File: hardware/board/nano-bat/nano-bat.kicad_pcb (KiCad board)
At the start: 2 copper layers, 160 x 106.7 mm, 97 parts, among them J101 Barrel_Jack_Switch, J102 USB_B_Mini, J103 Screw_Terminal_01x02, J104 Conn_01x02, J201 Conn_2Rows-45Pins, J301 Conn_ARM_JTAG_SWD_10, J302 Conn_01x10, J303 Conn_01x10, Q101 Q_PMOS_GSD, Q501 Q_PMOS_GSD, Q502 Q_NMOS_GSD, Q503 Q_NMOS_GSD, SW301 SW_Push, SW302 SW_Push, SW303 SW_Push, SW304 SW_Push, U201 AP3032, U301 M95256-WMN6P, U302 STM32L452CEUx, U401 LTC2942, U501 MIC2104YML-TR, U502 MCP1702

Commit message: Adding test points, initial board outline
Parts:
- added F401: Polyfuse, Fuse:Fuse_0603_1608Metric, F.Cu at (227.3, 78.2)
- added F501: Polyfuse, Fuse:Fuse_1812_4532Metric, F.Cu at (222.9, 120.7)
- added R315: 40.2k, Resistor_SMD:R_0603_1608Metric, F.Cu at (180.1, 23.0)
- added R316: 10k, Resistor_SMD:R_0603_1608Metric, F.Cu at (180.1, 25.5)
- added TP301: TestPoint, TestPoint:TestPoint_Plated_Hole_D2.0mm, F.Cu at (175.8, 24.1)
- J102: footprint footprints:USB-MICRO-B-HIROSE-UX60-MB-5S8 -> Connector_USB:USB_Mini-B_Lumberg_2486_01_Horizontal
- R406: footprint footprints:SM6227 -> Resistor_SMD:R_1206_3216Metric
- U201: moved to B.Cu
- moved C202 185.7 mm to (121.1, 134.0)
- moved D201 185.7 mm to (117.0, 131.7)
- moved L201 185.7 mm to (112.6, 131.7)
- moved R201 185.7 mm to (121.1, 131.4)
- moved C201 185.7 mm to (125.1, 131.4)
- moved U302 181.7 mm to (143.9, 33.7)
- moved U201 171.2 mm to (120.7, 123.8)
- moved J102 150.4 mm to (178.4, 58.4), turned to 180 degrees
- moved J104 140.0 mm to (196.2, 74.3), turned to 90 degrees
- moved J301 128.0 mm to (143.5, 22.9)
- moved J103 124.3 mm to (196.2, 86.4), turned to 90 degrees
- moved C302 117.9 mm to (155.4, 41.0)
- moved C305 117.9 mm to (155.4, 38.5)
- moved C311 117.9 mm to (164.0, 41.5)
- moved C301 117.9 mm to (164.6, 31.5)
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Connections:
- C201 pad 1: +2V8 -> GND
- C202 pad 2: +2V8 -> GND
- C301 pad 2: +2V8 -> GND
- C302 pad 2: +2V8 -> GND
- C303 pad 2: +2V8 -> GND
- C304 pad 2: +2V8 -> GND
- C305 pad 1: +2V8 -> GND
- C308 pad 2: +2V8 -> GND
- C309 pad 2: +2V8 -> GND
- C310 pad 2: +2V8 -> GND
- C311 pad 2: +2V8 -> GND
- C312 pad 2: +2V8 -> GND
- C401 pad 1: +2V8 -> GND
- C402 pad 2: +2V8 -> GND
- C503 pad 1: Net-(C503-Pad1) -> GND
- C504 pad 1: +2V8 -> GND
- C505 pad 2: +2V8 -> GND
- C506 pad 2: +2V8 -> GND
- C509 pad 1: /Coulomb Counter/Vbatt_source -> Net-(C509-Pad1)
- C510 pad 1: /Coulomb Counter/Vbatt_source -> Net-(C509-Pad1)
- C510 pad 2: +2V8 -> GND
- D102 pad 1: +2V8 -> GND
- FB101 pad 1: +2V8 -> GND
- FB102 pad 2: +2V8 -> GND
- FB301 pad 2: +2V8 -> GND
- J103 pad 2: +2V8 -> GND
- J104 pad 2: +2V8 -> GND
- J201 pad 10: +2V8 -> GND
- J201 pad 11: +2V8 -> GND
- J201 pad 12: +2V8 -> GND
- J201 pad 13: +2V8 -> GND
- J201 pad 14: +2V8 -> GND
- J201 pad 15: +2V8 -> GND
- J201 pad 16: +2V8 -> GND
- J201 pad 17: +2V8 -> GND
- J201 pad 18: +2V8 -> GND
- J201 pad 19: +2V8 -> GND
- J201 pad 2: +2V8 -> GND
- J201 pad 20: +2V8 -> GND
- J201 pad 21: +2V8 -> GND
- J201 pad 22: +2V8 -> GND
- J201 pad 23: +2V8 -> GND
- J201 pad 24: +2V8 -> GND
- J201 pad 25: +2V8 -> GND
- J201 pad 26: +2V8 -> GND
- J201 pad 27: +2V8 -> GND
- J201 pad 28: +2V8 -> GND
- J201 pad 33: +2V8 -> /(Opt) TFT Display/D~CX
- J201 pad 38: +2V8 -> GND
- J201 pad 39: +2V8 -> GND
- J201 pad 7: +2V8 -> GND
- J201 pad 8: +2V8 -> GND
- J201 pad 9: +2V8 -> GND
- J301 pad 3: +2V8 -> GND
- J301 pad 5: +2V8 -> GND
- J301 pad 9: +2V8 -> GND
- J302 pad 1: +2V8 -> GND
- J302 pad 10: +2V8 -> GND
- J302 pad 4: /Microcontroller/CC_~AL~CC -> /Microcontroller/Vadj
- J303 pad 1: +2V8 -> GND
- J303 pad 10: +2V8 -> GND
- J303 pad 3: /Microcontroller/PA8 -> /Microcontroller/PB8
- J303 pad 4: /Microcontroller/PB8 -> /Microcontroller/PB9
- L501 pad 2: /Coulomb Counter/Vbatt_source -> Net-(C509-Pad1)
- NT501 pad 2: +2V8 -> GND
- R102 pad 2: +2V8 -> GND
- R201 pad 2: +2V8 -> GND
- R406 pad 2: /Coulomb Counter/Vbatt_source -> Net-(F401-Pad1)
- R503 pad 2: +2V8 -> GND
- R506 pad 2: /Coulomb Counter/Vbatt_source -> Net-(C509-Pad1)
- R507 pad 1: +2V8 -> GND
- SW301 pad 2: +2V8 -> GND
- SW302 pad 2: +2V8 -> GND
- SW303 pad 2: +2V8 -> GND
- SW304 pad 2: +2V8 -> GND
- U201 pad 2: +2V8 -> GND
- U301 pad 4: +2V8 -> GND
- U302 pad 10: /Microcontroller/CC_~AL~CC -> Net-(R315-Pad2)
- U302 pad 21: +2V8 -> /(Opt) TFT Display/D~CX
- U302 pad 23: +2V8 -> GND
- U302 pad 29: /Microcontroller/PA8 -> /Microcontroller/CC_~AL~CC
- U302 pad 35: +2V8 -> GND
- U302 pad 46: Net-(U302-Pad46) -> /Microcontroller/PB9
- U302 pad 47: +2V8 -> GND
- U302 pad 49: +2V8 -> GND
- U401 pad 1: /Coulomb Counter/Vbatt_source -> Net-(F401-Pad1)
- U401 pad 2: +2V8 -> GND
- U501 pad 12: Net-(C503-Pad1) -> GND
- U502 pad 1: +2V8 -> GND
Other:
- board size 160 x 106.7 mm -> 78.1 x 62.2 mm

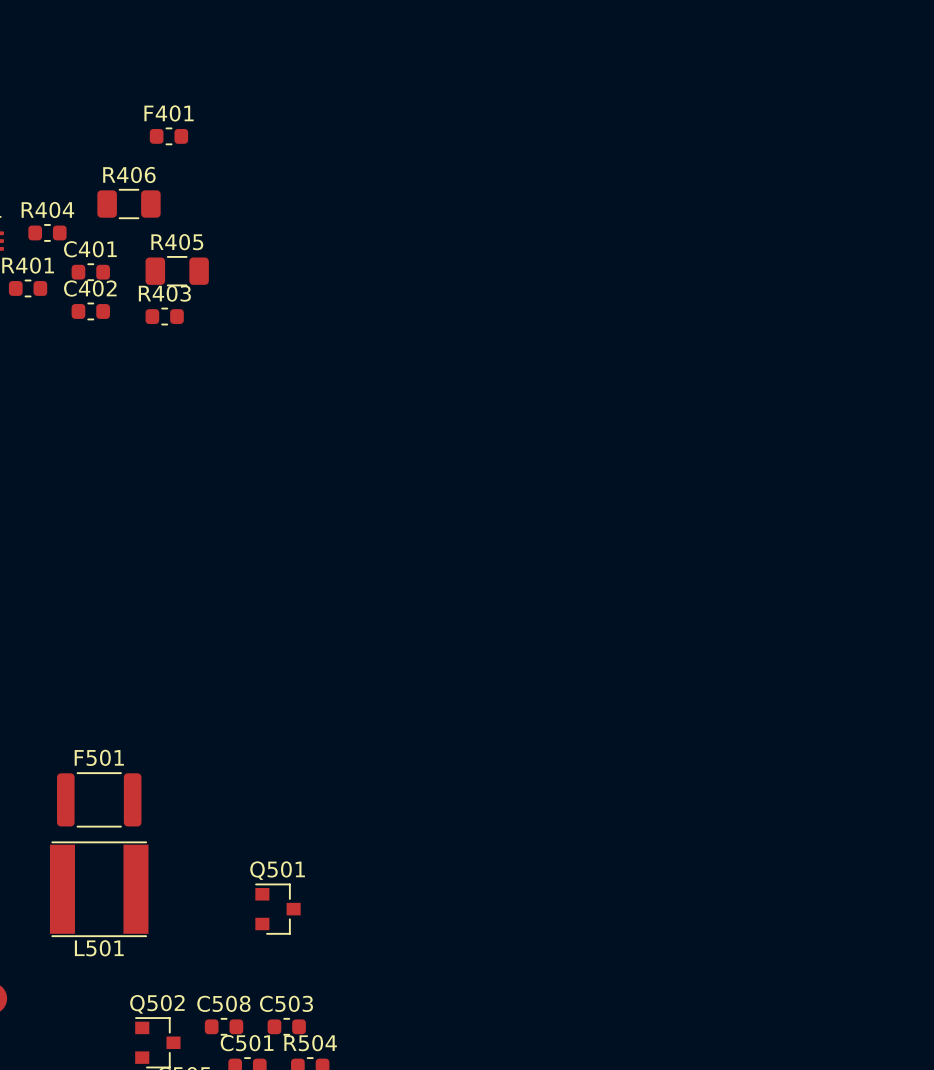
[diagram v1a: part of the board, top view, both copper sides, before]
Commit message: Updating test points, adding 3d models
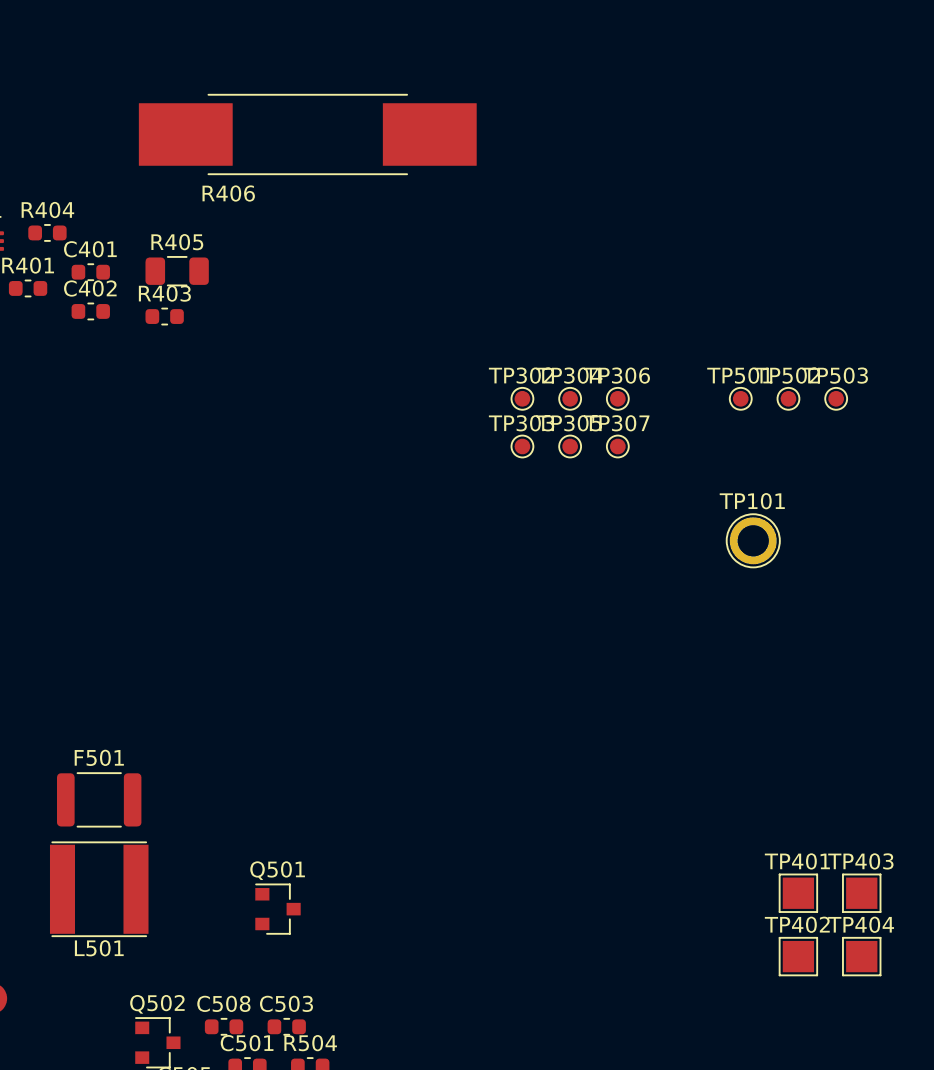
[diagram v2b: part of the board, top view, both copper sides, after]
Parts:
- removed F401: Polyfuse, Fuse:Fuse_0603_1608Metric
- added TP101: TestPoint, TestPoint:TestPoint_Plated_Hole_D2.0mm, F.Cu at (264.7, 104.1)
- added TP302: TestPoint, TestPoint:TestPoint_Pad_D1.0mm, F.Cu at (249.9, 95.0)
- added TP303: TestPoint, TestPoint:TestPoint_Pad_D1.0mm, F.Cu at (249.9, 98.1)
- added TP304: TestPoint, TestPoint:TestPoint_Pad_D1.0mm, F.Cu at (253.0, 95.0)
- added TP305: TestPoint, TestPoint:TestPoint_Pad_D1.0mm, F.Cu at (253.0, 98.1)
- added TP306: TestPoint, TestPoint:TestPoint_Pad_D1.0mm, F.Cu at (256.0, 95.0)
- added TP307: TestPoint, TestPoint:TestPoint_Pad_D1.0mm, F.Cu at (256.0, 98.1)
- added TP401: TestPoint, TestPoint:TestPoint_Pad_2.0x2.0mm, F.Cu at (267.6, 126.6)
- added TP402: TestPoint, TestPoint:TestPoint_Pad_2.0x2.0mm, F.Cu at (267.6, 130.7)
- added TP403: TestPoint, TestPoint:TestPoint_Pad_2.0x2.0mm, F.Cu at (271.6, 126.6)
- added TP404: TestPoint, TestPoint:TestPoint_Pad_2.0x2.0mm, F.Cu at (271.6, 130.7)
- added TP501: TestPoint, TestPoint:TestPoint_Pad_D1.0mm, F.Cu at (263.9, 95.0)
- added TP502: TestPoint, TestPoint:TestPoint_Pad_D1.0mm, F.Cu at (267.0, 95.0)
- added TP503: TestPoint, TestPoint:TestPoint_Pad_D1.0mm, F.Cu at (270.0, 95.0)
- R406: footprint Resistor_SMD:R_1206_3216Metric -> footprints:SM6227
- moved R406 12.3 mm to (236.2, 78.1)
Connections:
- J302 pad 2: +2V8 -> /Microcontroller/CC_SCL
- J302 pad 3: Net-(J302-Pad3) -> /Microcontroller/CC_SDA
- J302 pad 9: +2V8 -> /Microcontroller/PB8
- J303 pad 3: /Microcontroller/PB8 -> /Microcontroller/PB9
- J303 pad 4: /Microcontroller/PB9 -> /(Opt) TFT Display/D~CX
- R406 pad 2: Net-(F401-Pad1) -> /Coulomb Counter/Vbatt_source
- U401 pad 1: Net-(F401-Pad1) -> /Coulomb Counter/Vbatt_source
